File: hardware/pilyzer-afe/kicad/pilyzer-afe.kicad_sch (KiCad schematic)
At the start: 32 parts, among them J5 Logic D0–D7 + GND, J6 Pico 2 socket, J7 Pico 2 socket, U1 TLV9064IDR, U2 TS5A23159DGSR

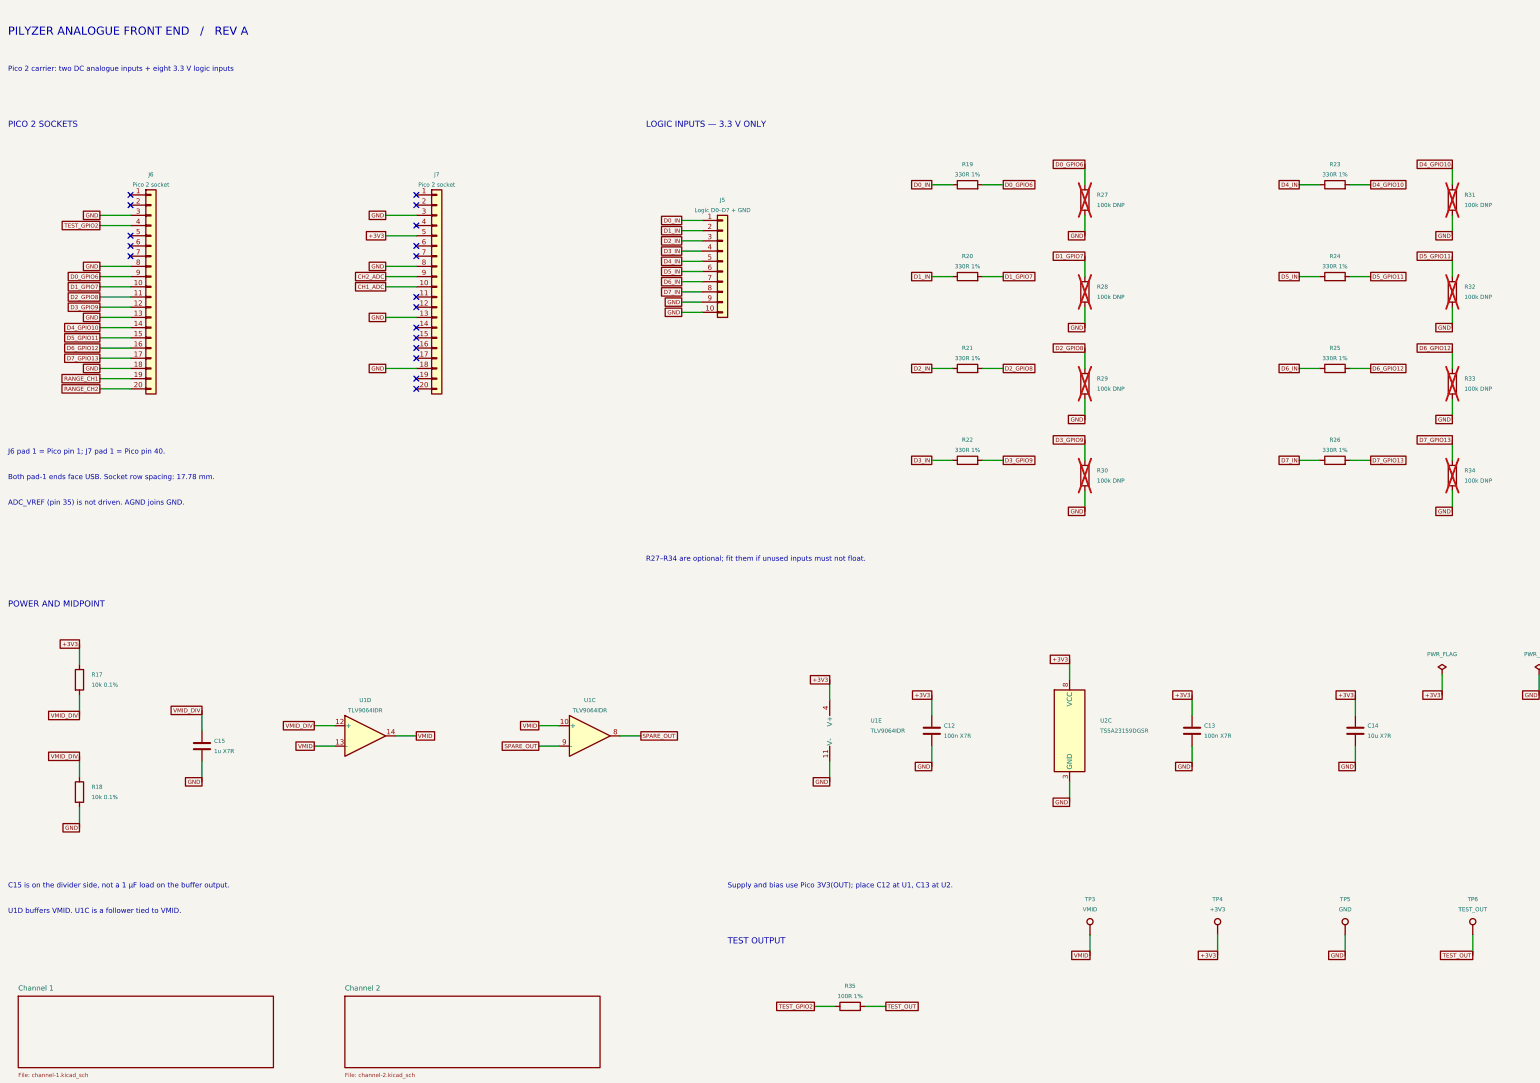
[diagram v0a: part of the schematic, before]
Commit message: Add complementary chord outputs and remap GPIOs with nine-pin J8
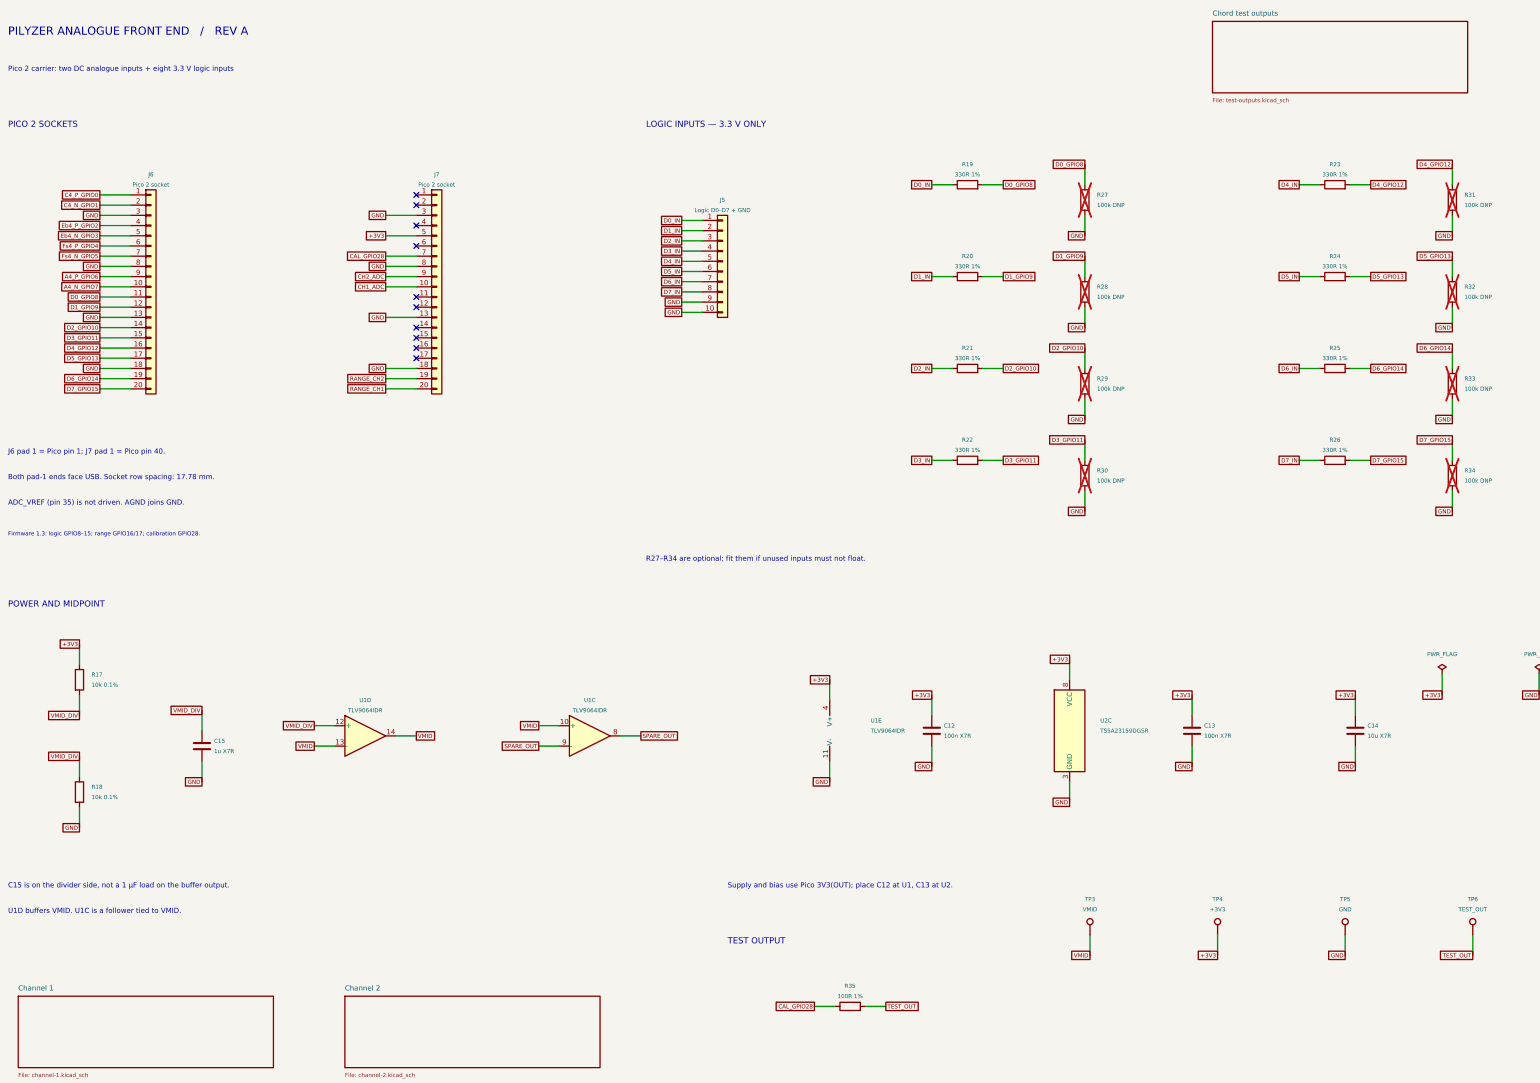
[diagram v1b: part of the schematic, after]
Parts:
- removed TP3: VMID, PiLyzer:TestPoint_Plated_Hole_D2.0mm, symbol PiLyzer:Connector_TestPoint
- removed TP4: +3V3, PiLyzer:TestPoint_Plated_Hole_D2.0mm, symbol PiLyzer:Connector_TestPoint
- added TP5: GND, PiLyzer:TestPoint_Plated_Hole_D2.0mm, symbol PiLyzer:Connector_TestPoint
- added TP6: TEST_OUT, PiLyzer:TestPoint_Plated_Hole_D2.0mm, symbol PiLyzer:Connector_TestPoint
- TP3: renamed from TP5; value GND -> VMID
- TP4: renamed from TP6; value TEST_OUT -> +3V3
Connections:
- net +3V3: now also TP4.1
- net GND: now also TP5.1; no longer TP3.1
- net RANGE_CH1: now also J7.20 (Pin_20); no longer J6.19 (Pin_19)
- net RANGE_CH2: now also J7.19 (Pin_19); no longer J6.20 (Pin_20)
- net TEST_OUT: now also TP6.1; no longer TP4.1
- net VMID: now also TP3.1
- net C4_P_GPIO0: now reaches J6.1 (Pin_1)
- net C4_N_GPIO1: now reaches J6.2 (Pin_2)
- net Eb4_N_GPIO3: now reaches J6.5 (Pin_5)
- net Fs4_P_GPIO4: now reaches J6.6 (Pin_6)
- net Fs4_N_GPIO5: now reaches J6.7 (Pin_7)
- net CAL_GPIO28: now reaches J7.7 (Pin_7)
- net CAL_GPIO28: now also R35.1
- net D0_GPIO6 renamed D0_GPIO8
- net D0_GPIO8: now also J6.11 (Pin_11); no longer J6.9 (Pin_9)
- net D1_GPIO7 renamed D1_GPIO9
- net D1_GPIO9: now also J6.12 (Pin_12); no longer J6.10 (Pin_10)
- net D2_GPIO8 renamed D2_GPIO10
- net D2_GPIO10: now also J6.14 (Pin_14); no longer J6.11 (Pin_11)
- net D3_GPIO9 renamed D3_GPIO11
- net D3_GPIO11: now also J6.15 (Pin_15); no longer J6.12 (Pin_12)
- net D4_GPIO10 renamed D4_GPIO12
- net D4_GPIO12: now also J6.16 (Pin_16); no longer J6.14 (Pin_14)
- net D5_GPIO11 renamed D5_GPIO13
- net D5_GPIO13: now also J6.17 (Pin_17); no longer J6.15 (Pin_15)
- net D6_GPIO12 renamed D6_GPIO14
- net D6_GPIO14: now also J6.19 (Pin_19); no longer J6.16 (Pin_16)
- net D7_GPIO13 renamed D7_GPIO15
- net D7_GPIO15: now also J6.20 (Pin_20); no longer J6.17 (Pin_17)
- net TEST_GPIO2 renamed Eb4_P_GPIO2
- net Eb4_P_GPIO2: no longer R35.1
- new net A4_N_GPIO7: J6.10 (Pin_10)
- new net A4_P_GPIO6: J6.9 (Pin_9)
- no-connect marks 18 -> 10
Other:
- added sheet Chord test outputs (test-outputs.kicad_sch)
- note added: "Firmware 1.3: logic GPIO8–15; range GPIO16/17; calibration GPIO28."
- moved on the sheet: TP3, TP4

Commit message: Separate chord generator from PiLyzer and remove J8
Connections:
- net A4_N_GPIO7: no longer names the net of J6.10 (Pin_10)
- net A4_P_GPIO6: no longer names the net of J6.9 (Pin_9)
- net C4_N_GPIO1: no longer names the net of J6.2 (Pin_2)
- net C4_P_GPIO0: no longer names the net of J6.1 (Pin_1)
- net Eb4_N_GPIO3: no longer names the net of J6.5 (Pin_5)
- net Eb4_P_GPIO2: no longer names the net of J6.4 (Pin_4)
- net Fs4_N_GPIO5: no longer names the net of J6.7 (Pin_7)
- net Fs4_P_GPIO4: no longer names the net of J6.6 (Pin_6)
- no-connect marks 10 -> 18
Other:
- removed sheet Chord test outputs
- note added: "Firmware 1.4: logic GPIO8–15; range GPIO16/17; calibration GPIO28."
- note removed: "Firmware 1.3: logic GPIO8–15; range GPIO16/17; calibration GPIO28."
